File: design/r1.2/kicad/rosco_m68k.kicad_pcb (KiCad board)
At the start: 4 copper layers, 160 x 100 mm, 81 parts, among them IC1 MC68010P10, IC2 ATF16V8BQL-15PU, IC3 ATF16V8BQL-15PU, IC4 MC68901P, IC5 ATF16V8BQL-15PU, IC6 74174N, IC8 555N, IC9 74LS01N, J1 PWR, J2 Conn_01x06, J3 Conn_02x32_Odd_Even, J5 GPIO-PANEL, Q1 3.6864MHz, Q2 5H8ET-10.000, Q3 5H8ET-4.000, U1 AT28C256-15PU, U2 AT28C256-15PU, U3 AS6C4008-55PCN, U4 AS6C4008-55PCN, U5 74LS93

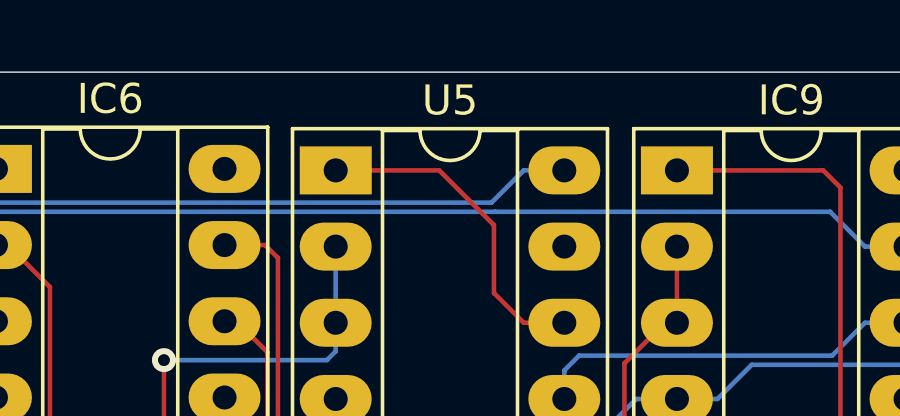
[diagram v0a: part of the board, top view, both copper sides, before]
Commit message: Fix 1.21 incorrect IC7 ref (was U5)
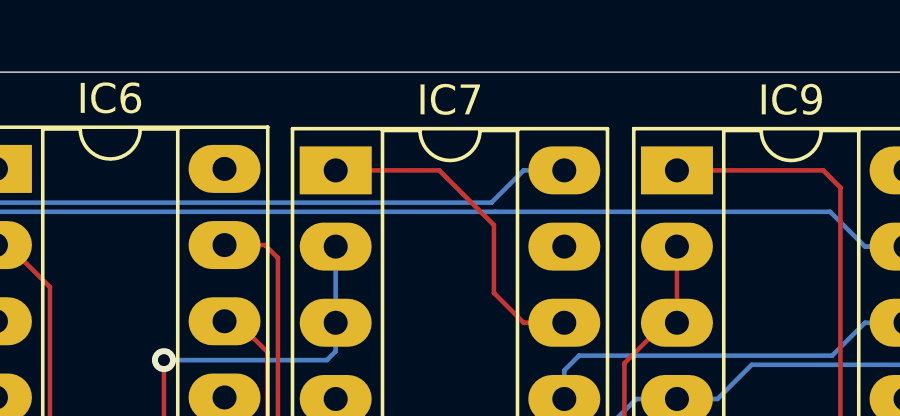
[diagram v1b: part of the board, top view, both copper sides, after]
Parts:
- renumbered U5 to IC7
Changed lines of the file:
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@@
   )
   (setup
-    (last_trace_width 0.1524)
+    (last_trace_width 0.25)
     (user_trace_width 0.1524)
     (user_trace_width 0.65)
@@
   (net 121 "Net-(R12-Pad2)")
   (net 122 /Expansion/A17)
-  (net 123 "Net-(IC9-Pad11)")
-  (net 124 "Net-(U5-Pad1)")
-  (net 125 "Net-(U5-Pad8)")
-  (net 126 "Net-(U5-Pad9)")
+  (net 123 "Net-(IC7-Pad1)")
+  (net 124 "Net-(IC7-Pad8)")
+  (net 125 "Net-(IC7-Pad9)")
+  (net 126 "Net-(IC7-Pad11)")
   (net_class Default "This is the default net class."
     (clearance 0.1524)
@@
     (add_net "Net-(IC6-Pad2)")
     (add_net "Net-(IC6-Pad5)")
+    (add_net "Net-(IC7-Pad1)")
+    (add_net "Net-(IC7-Pad11)")
+    (add_net "Net-(IC7-Pad8)")
+    (add_net "Net-(IC7-Pad9)")
     (add_net "Net-(IC8-Pad3)")
     (add_net "Net-(IC8-Pad7)")
     (add_net "Net-(IC9-Pad10)")
-    (add_net "Net-(IC9-Pad11)")
     (add_net "Net-(J2-Pad3)")
     (add_net "Net-(J2-Pad6)")
@@
     (add_net "Net-(S1-Pad2)")
     (add_net "Net-(S1-Pad4)")
-    (add_net "Net-(U5-Pad1)")
-    (add_net "Net-(U5-Pad8)")
-    (add_net "Net-(U5-Pad9)")
     (add_net ODDRAMSEL)
     (add_net ODDROMSEL)
@@
     (descr "14-lead though-hole mounted DIP package, row spacing 7.62 mm (300 mils), Socket, LongPads")
     (tags "THT DIP DIL PDIP 2.54mm 7.62mm 300mil Socket LongPads")
-    (fp_text reference U5 (at 3.81 -2.33) (layer F.SilkS)
+    (fp_text reference IC7 (at 3.81 -2.33) (layer F.SilkS)
       (effects (font (size 1 1) (thickness 0.15)))
     )
@@
     )
     (pad 1 thru_hole rect (at 0 0) (size 2.4 1.6) (drill 0.8) (layers *.Cu *.Mask)
-      (net 124 "Net-(U5-Pad1)"))
+      (net 123 "Net-(IC7-Pad1)"))
     (pad 8 thru_hole oval (at 7.62 15.24) (size 2.4 1.6) (drill 0.8) (layers *.Cu *.Mask)
-      (net 125 "Net-(U5-Pad8)"))
+      (net 124 "Net-(IC7-Pad8)"))
     (pad 2 thru_hole oval (at 0 2.54) (size 2.4 1.6) (drill 0.8) (layers *.Cu *.Mask)
       (net 12 AS))
     (pad 9 thru_hole oval (at 7.62 12.7) (size 2.4 1.6) (drill 0.8) (layers *.Cu *.Mask)
-      (net 126 "Net-(U5-Pad9)"))
+      (net 125 "Net-(IC7-Pad9)"))
     (pad 3 thru_hole oval (at 0 5.08) (size 2.4 1.6) (drill 0.8) (layers *.Cu *.Mask)
       (net 12 AS))
@@
     (pad 4 thru_hole oval (at 0 7.62) (size 2.4 1.6) (drill 0.8) (layers *.Cu *.Mask))
     (pad 11 thru_hole oval (at 7.62 7.62) (size 2.4 1.6) (drill 0.8) (layers *.Cu *.Mask)
-      (net 123 "Net-(IC9-Pad11)"))
+      (net 126 "Net-(IC7-Pad11)"))
     (pad 5 thru_hole oval (at 0 10.16) (size 2.4 1.6) (drill 0.8) (layers *.Cu *.Mask)
       (net 17 VCC))
     (pad 12 thru_hole oval (at 7.62 5.08) (size 2.4 1.6) (drill 0.8) (layers *.Cu *.Mask)
-      (net 124 "Net-(U5-Pad1)"))
+      (net 123 "Net-(IC7-Pad1)"))
     (pad 6 thru_hole oval (at 0 12.7) (size 2.4 1.6) (drill 0.8) (layers *.Cu *.Mask))
     (pad 13 thru_hole oval (at 7.62 2.54) (size 2.4 1.6) (drill 0.8) (layers *.Cu *.Mask))
@@
       (net 7 RESET))
     (pad 11 thru_hole oval (at 7.62 7.62) (size 2.4 1.6) (drill 0.8) (layers *.Cu *.Mask)
-      (net 123 "Net-(IC9-Pad11)"))
+      (net 126 "Net-(IC7-Pad11)"))
     (pad 5 thru_hole oval (at 0 10.16) (size 2.4 1.6) (drill 0.8) (layers *.Cu *.Mask)
       (net 42 "Net-(IC8-Pad3)"))
     (pad 12 thru_hole oval (at 7.62 5.08) (size 2.4 1.6) (drill 0.8) (layers *.Cu *.Mask)
-      (net 123 "Net-(IC9-Pad11)"))
+      (net 126 "Net-(IC7-Pad11)"))
     (pad 6 thru_hole oval (at 0 12.7) (size 2.4 1.6) (drill 0.8) (layers *.Cu *.Mask)
       (net 42 "Net-(IC8-Pad3)"))
@@
   (segment (start 110.375 102.413) (end 110.398 102.39) (width 0.1524) (layer Top) (net 122))
   (segment (start 110.375 104.975) (end 110.375 102.413) (width 0.1524) (layer Top) (net 122))
-  (segment (start 203.4176 63.4548) (end 202.3224 64.55) (width 0.1524) (layer Bottom) (net 123))
-  (segment (start 204.77 63.4548) (end 203.4176 63.4548) (width 0.1524) (layer Bottom) (net 123))
-  (segment (start 193.395 65.0424) (end 193.395 65.9948) (width 0.1524) (layer Bottom) (net 123))
-  (segment (start 193.8874 64.55) (end 193.395 65.0424) (width 0.1524) (layer Bottom) (net 123))
-  (segment (start 202.3224 64.55) (end 193.8874 64.55) (width 0.1524) (layer Bottom) (net 123))
-  (segment (start 204.77 64.4072) (end 204.77 65.9948) (width 0.1524) (layer Top) (net 123))
-  (segment (start 204.77 63.4548) (end 204.77 64.4072) (width 0.1524) (layer Top) (net 123))
-  (segment (start 192.0426 63.4548) (end 191.05 62.4622) (width 0.1524) (layer Top) (net 124))
-  (segment (start 193.395 63.4548) (end 192.0426 63.4548) (width 0.1524) (layer Top) (net 124))
-  (segment (start 191.05 62.4622) (end 191.05 60.2) (width 0.1524) (layer Top) (net 124))
-  (segment (start 189.2248 58.3748) (end 185.775 58.3748) (width 0.1524) (layer Top) (net 124))
-  (segment (start 191.05 60.2) (end 189.2248 58.3748) (width 0.1524) (layer Top) (net 124))
+  (segment (start 203.4176 63.4548) (end 202.3224 64.55) (width 0.1524) (layer Bottom) (net 126))
+  (segment (start 204.77 63.4548) (end 203.4176 63.4548) (width 0.1524) (layer Bottom) (net 126))
+  (segment (start 193.395 65.0424) (end 193.395 65.9948) (width 0.1524) (layer Bottom) (net 126))
+  (segment (start 193.8874 64.55) (end 193.395 65.0424) (width 0.1524) (layer Bottom) (net 126))
+  (segment (start 202.3224 64.55) (end 193.8874 64.55) (width 0.1524) (layer Bottom) (net 126))
+  (segment (start 204.77 64.4072) (end 204.77 65.9948) (width 0.1524) (layer Top) (net 126))
+  (segment (start 204.77 63.4548) (end 204.77 64.4072) (width 0.1524) (layer Top) (net 126))
+  (segment (start 192.0426 63.4548) (end 191.05 62.4622) (width 0.1524) (layer Top) (net 123))
+  (segment (start 193.395 63.4548) (end 192.0426 63.4548) (width 0.1524) (layer Top) (net 123))
+  (segment (start 191.05 62.4622) (end 191.05 60.2) (width 0.1524) (layer Top) (net 123))
+  (segment (start 189.2248 58.3748) (end 185.775 58.3748) (width 0.1524) (layer Top) (net 123))
+  (segment (start 191.05 60.2) (end 189.2248 58.3748) (width 0.1524) (layer Top) (net 123))
   (zone (net 18) (net_name GND) (layer Route2) (hatch edge 0.508)
     (connect_pads (clearance 0.508))

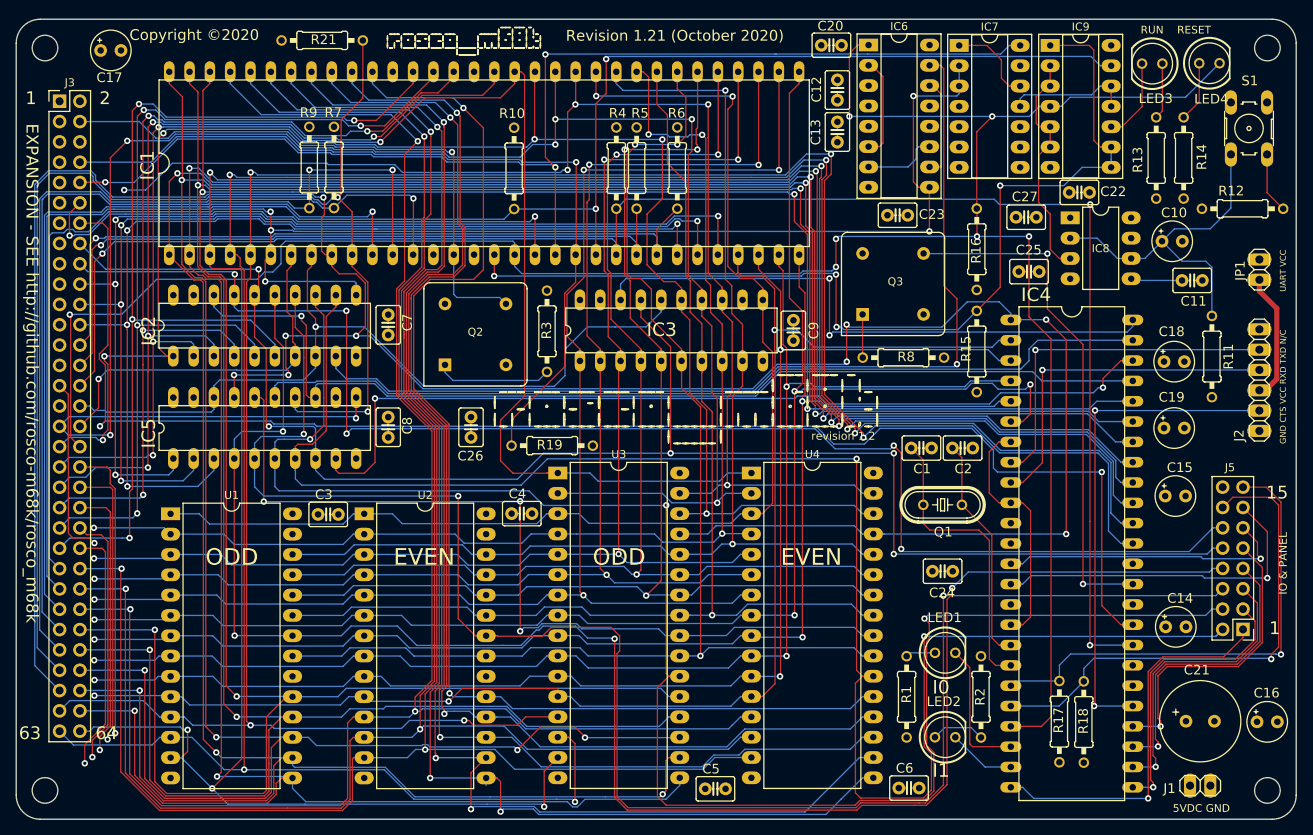
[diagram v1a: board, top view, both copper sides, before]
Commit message: Board changes for new DTACK
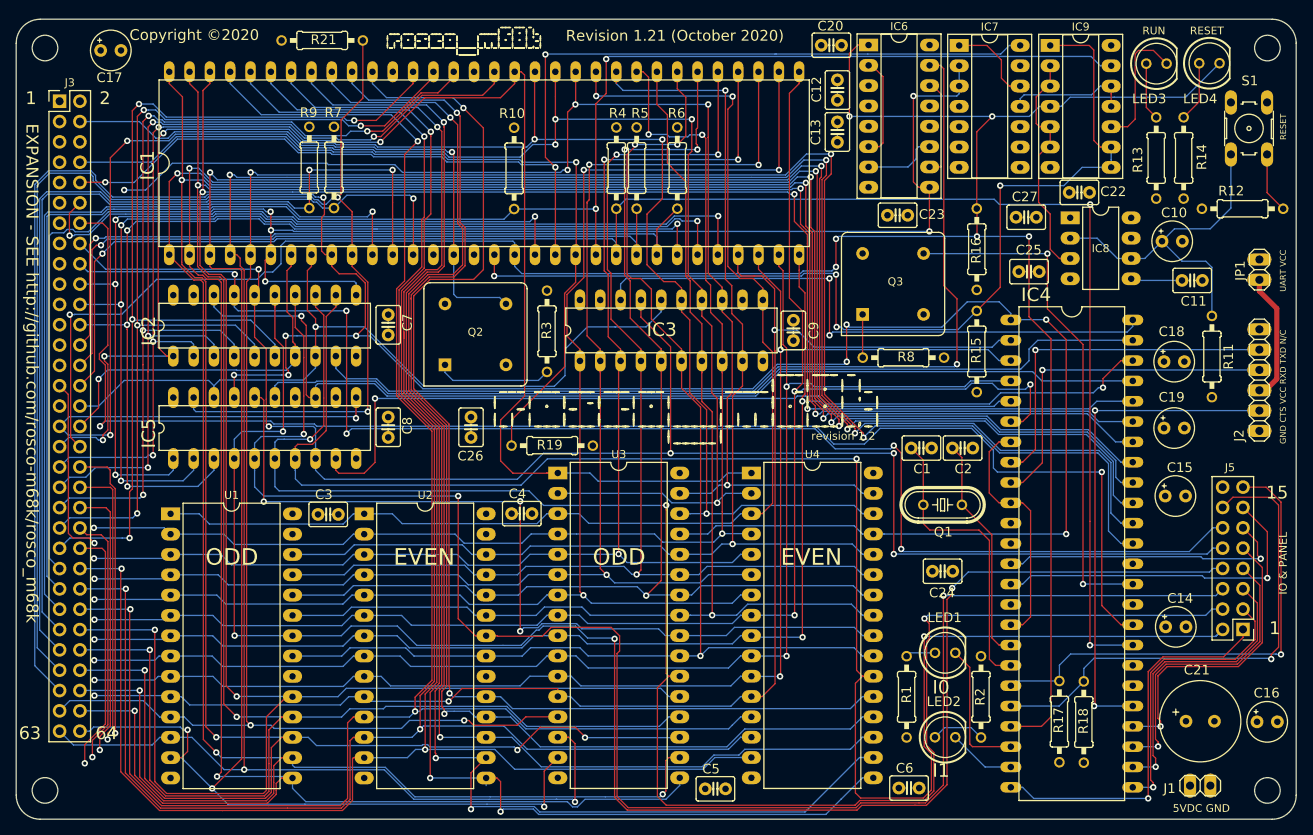
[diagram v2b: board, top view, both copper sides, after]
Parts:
- moved LED3 0.53 mm to (210.4, 60.6), turned to 0 degrees
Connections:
- IC5 pad 14: DTACK -> Net-(IC5-Pad14)
- IC5 pad 19: Net-(IC5-Pad19) -> DTACK
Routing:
- net DTACK: track 162.4 -> 175.1 mm
- net Net-(IC9-Pad10): track 10.3 -> 16.3 mm
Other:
- board text added: "RESET"
- board text added: "RUN"
- board text removed: "RUN RESET"
